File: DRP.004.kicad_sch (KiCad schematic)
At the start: 4 parts

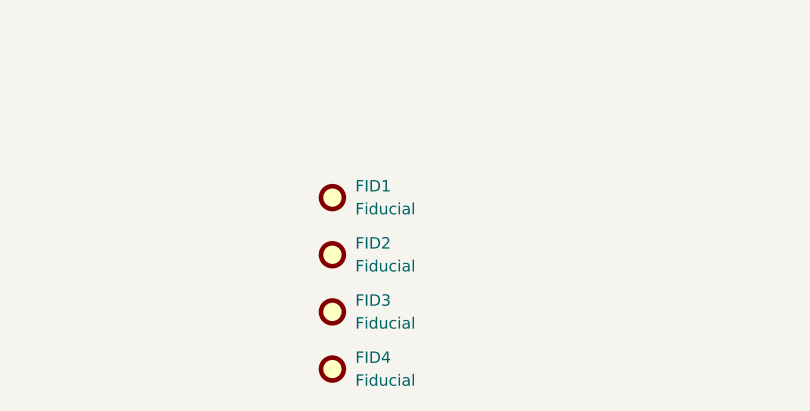
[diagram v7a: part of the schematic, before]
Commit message: V4 revision - Moved usb to HID side - Changed battery connector to ph2.0 with standard(ish) pinout - Better footprints for debug and ldr connectors - Changed switch from SK12D07 to MSK12C02 - Changed R(ILIM) to 1.1k - Better placement of servo power and connector - Changed thermistor to 0402 SMD - Removed jumper to NTC
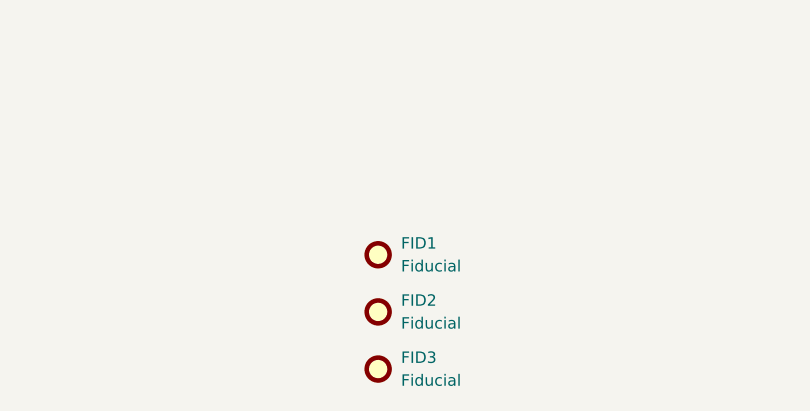
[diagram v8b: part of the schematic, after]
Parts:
- removed FID4: Fiducial, Fiducial:Fiducial_0.5mm_Mask1.5mm, symbol Mechanical:Fiducial
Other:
- moved on the sheet: FID1, FID2, FID3
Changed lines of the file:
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@@
 		(title "DRP.004")
 		(date "2025-04-05")
-		(rev "v3")
+		(rev "v4")
 		(company "SaintCarbonara")
 		(comment 1 "QUACK-QUACK, MAFAKA!")
@@
 	(symbol
 		(lib_id "Mechanical:Fiducial")
-		(at 157.48 180.34 0)
+		(at 162.56 186.69 0)
 		(unit 1)
 		(exclude_from_sim no)
@@
 		(fields_autoplaced yes)
 		(property "Reference" "FID2"
-			(at 160.02 179.0699 0)
+			(at 165.1 185.4199 0)
 			(effects
 				(font
@@
 		)
 		(property "Value" "Fiducial"
-			(at 160.02 181.6099 0)
+			(at 165.1 187.9599 0)
 			(effects
 				(font
@@
 		)
 		(property "Footprint" "Fiducial:Fiducial_0.5mm_Mask1.5mm"
-			(at 157.48 180.34 0)
+			(at 162.56 186.69 0)
 			(effects
 				(font
@@
 		)
 		(property "Datasheet" "~"
-			(at 157.48 180.34 0)
+			(at 162.56 186.69 0)
 			(effects
 				(font
@@
 		)
 		(property "Description" "Fiducial Marker"
-			(at 157.48 180.34 0)
+			(at 162.56 186.69 0)
 			(effects
 				(font
@@
 		)
 		(property "Tolerance " ""
-			(at 157.48 180.34 0)
+			(at 162.56 186.69 0)
 			(effects
 				(font
@@
 	(symbol
 		(lib_id "Mechanical:Fiducial")
-		(at 157.48 186.69 0)
+		(at 162.56 193.04 0)
 		(unit 1)
 		(exclude_from_sim no)
@@
 		(fields_autoplaced yes)
 		(property "Reference" "FID3"
-			(at 160.02 185.4199 0)
+			(at 165.1 191.7699 0)
 			(effects
 				(font
@@
 		)
 		(property "Value" "Fiducial"
-			(at 160.02 187.9599 0)
+			(at 165.1 194.3099 0)
 			(effects
 				(font
@@
 		)
 		(property "Footprint" "Fiducial:Fiducial_0.5mm_Mask1.5mm"
-			(at 157.48 186.69 0)
+			(at 162.56 193.04 0)
 			(effects
 				(font
@@
 		)
 		(property "Datasheet" "~"
-			(at 157.48 186.69 0)
+			(at 162.56 193.04 0)
 			(effects
 				(font
@@
 		)
 		(property "Description" "Fiducial Marker"
-			(at 157.48 186.69 0)
+			(at 162.56 193.04 0)
 			(effects
 				(font
@@
 		)
 		(property "Tolerance " ""
-			(at 157.48 186.69 0)
+			(at 162.56 193.04 0)
 			(effects
 				(font
@@
 	(symbol
 		(lib_id "Mechanical:Fiducial")
-		(at 157.48 173.99 0)
+		(at 162.56 180.34 0)
 		(unit 1)
 		(exclude_from_sim no)
@@
 		(fields_autoplaced yes)
 		(property "Reference" "FID1"
-			(at 160.02 172.7199 0)
+			(at 165.1 179.0699 0)
 			(effects
 				(font
@@
 		)
 		(property "Value" "Fiducial"
-			(at 160.02 175.2599 0)
+			(at 165.1 181.6099 0)
 			(effects
 				(font
@@
 		)
 		(property "Footprint" "Fiducial:Fiducial_0.5mm_Mask1.5mm"
-			(at 157.48 173.99 0)
+			(at 162.56 180.34 0)
 			(effects
 				(font
@@
 		)
 		(property "Datasheet" "~"
-			(at 157.48 173.99 0)
+			(at 162.56 180.34 0)
 			(effects
 				(font
@@
 		)
 		(property "Description" "Fiducial Marker"
-			(at 157.48 173.99 0)
+			(at 162.56 180.34 0)
 			(effects
 				(font
@@
 		)
 		(property "Tolerance " ""
-			(at 157.48 173.99 0)
+			(at 162.56 180.34 0)
 			(effects
 				(font
@@
 	)
 	(symbol
-		(lib_id "Mechanical:Fiducial")
-		(at 157.48 193.04 0)
-		(unit 1)
-		(exclude_from_sim no)
-		(in_bom no)
-		(on_board yes)
-		(dnp no)
-		(fields_autoplaced yes)
-		(property "Reference" "FID4"
-			(at 160.02 191.7699 0)
-			(effects
-				(font
-					(size 1.27 1.27)
-				)
-				(justify left)
-			)
-		)
-		(property "Value" "Fiducial"
-			(at 160.02 194.3099 0)
-			(effects
-				(font
-					(size 1.27 1.27)
-				)
-				(justify left)
-			)
-		)
-		(property "Footprint" "Fiducial:Fiducial_0.5mm_Mask1.5mm"
-			(at 157.48 193.04 0)
-			(effects
-				(font
-					(size 1.27 1.27)
-				)
-				(hide yes)
-			)
-		)
-		(property "Datasheet" "~"
-			(at 157.48 193.04 0)
-			(effects
-				(font
-					(size 1.27 1.27)
-				)
-				(hide yes)
-			)
-		)
-		(property "Description" "Fiducial Marker"
-			(at 157.48 193.04 0)
-			(effects
-				(font
-					(size 1.27 1.27)
-				)
-				(hide yes)
-			)
-		)
-		(property "Tolerance " ""
-			(at 157.48 193.04 0)
-			(effects
-				(font
-					(size 1.27 1.27)
-				)
-				(hide yes)
-			)
-		)
-		(instances
-			(project "DRP.004"
-				(path "/990f0ec4-1b5b-4db8-8f39-ecd88fffeea0"
-					(reference "FID4")
-					(unit 1)
-				)
-			)
-		)
-	)
-	(symbol
 		(lib_id "Graphic:SYM_Flash_Large")
 		(at 254 156.21 0)
@@
 			(at 254 156.21 0)
 			(effects
-				(font
-					(size 1.27 1.27)
-				)
-				(hide yes)
-			)
-		)
-		(property "Sim.Enable" "0"
-			(at 254 156.21 0)
-			(effects
